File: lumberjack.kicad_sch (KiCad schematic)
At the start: 156 parts

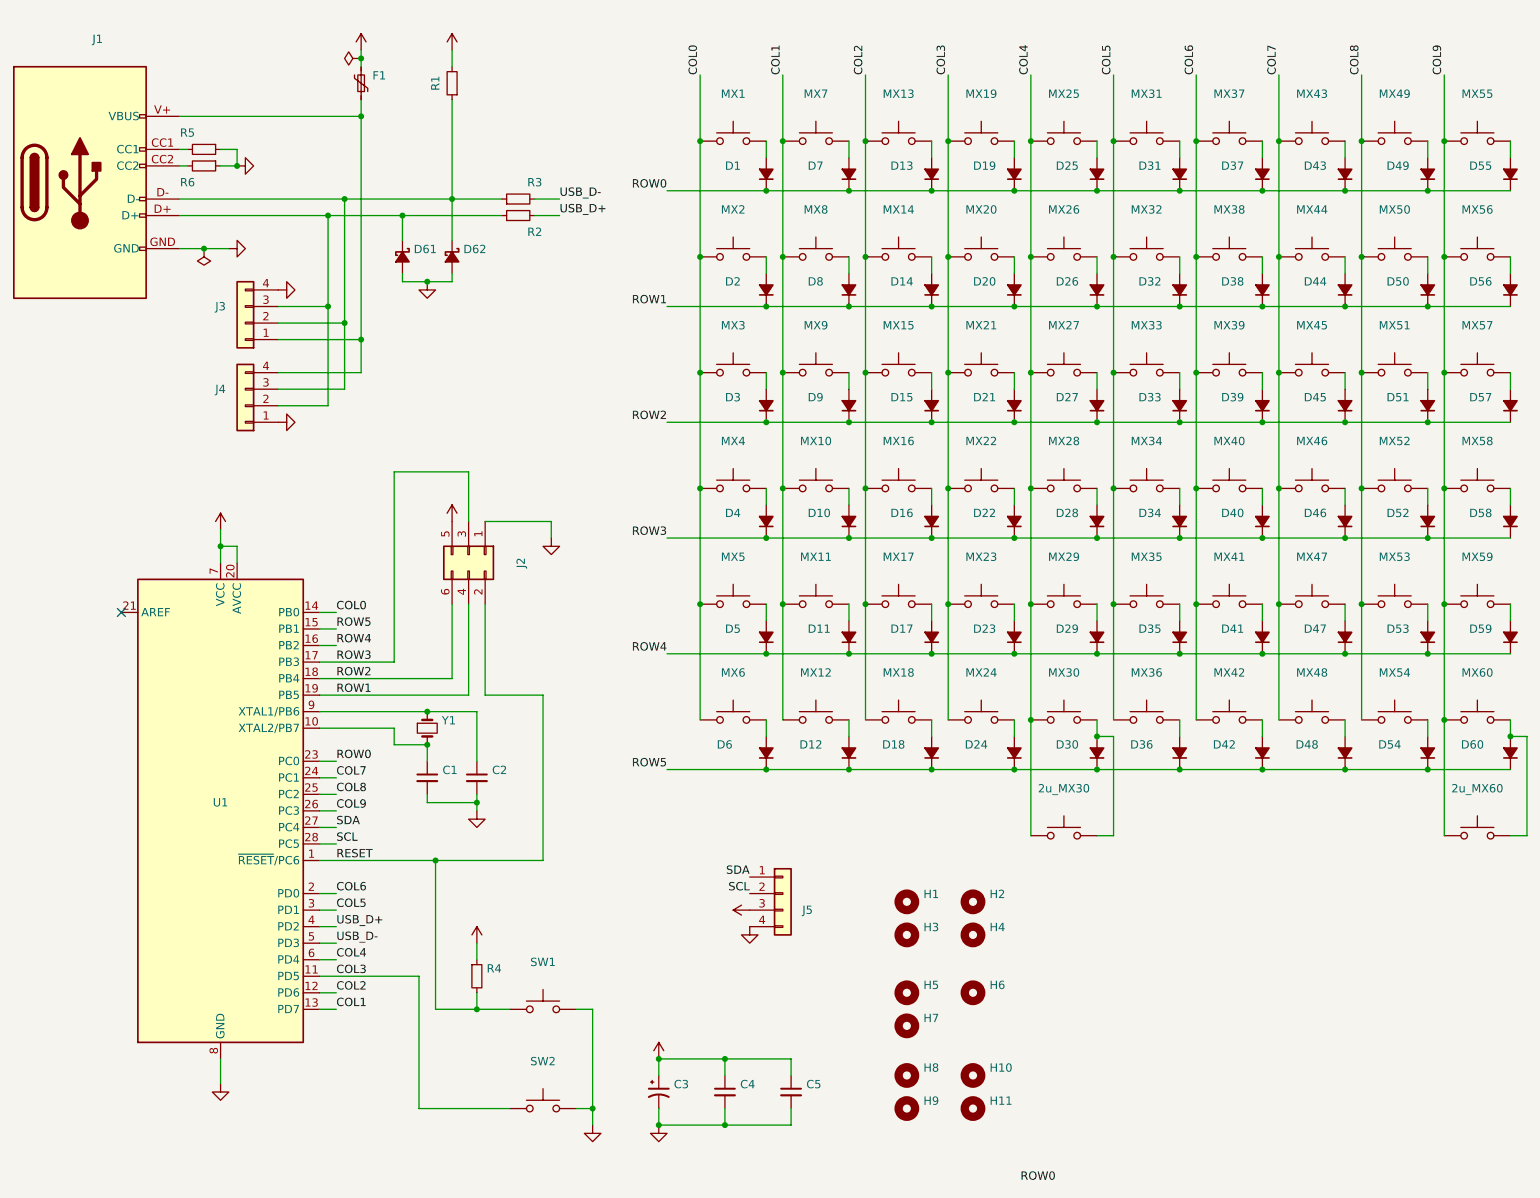
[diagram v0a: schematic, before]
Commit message: Revert to the correct version of the schematic, synchronize PCB with schematic
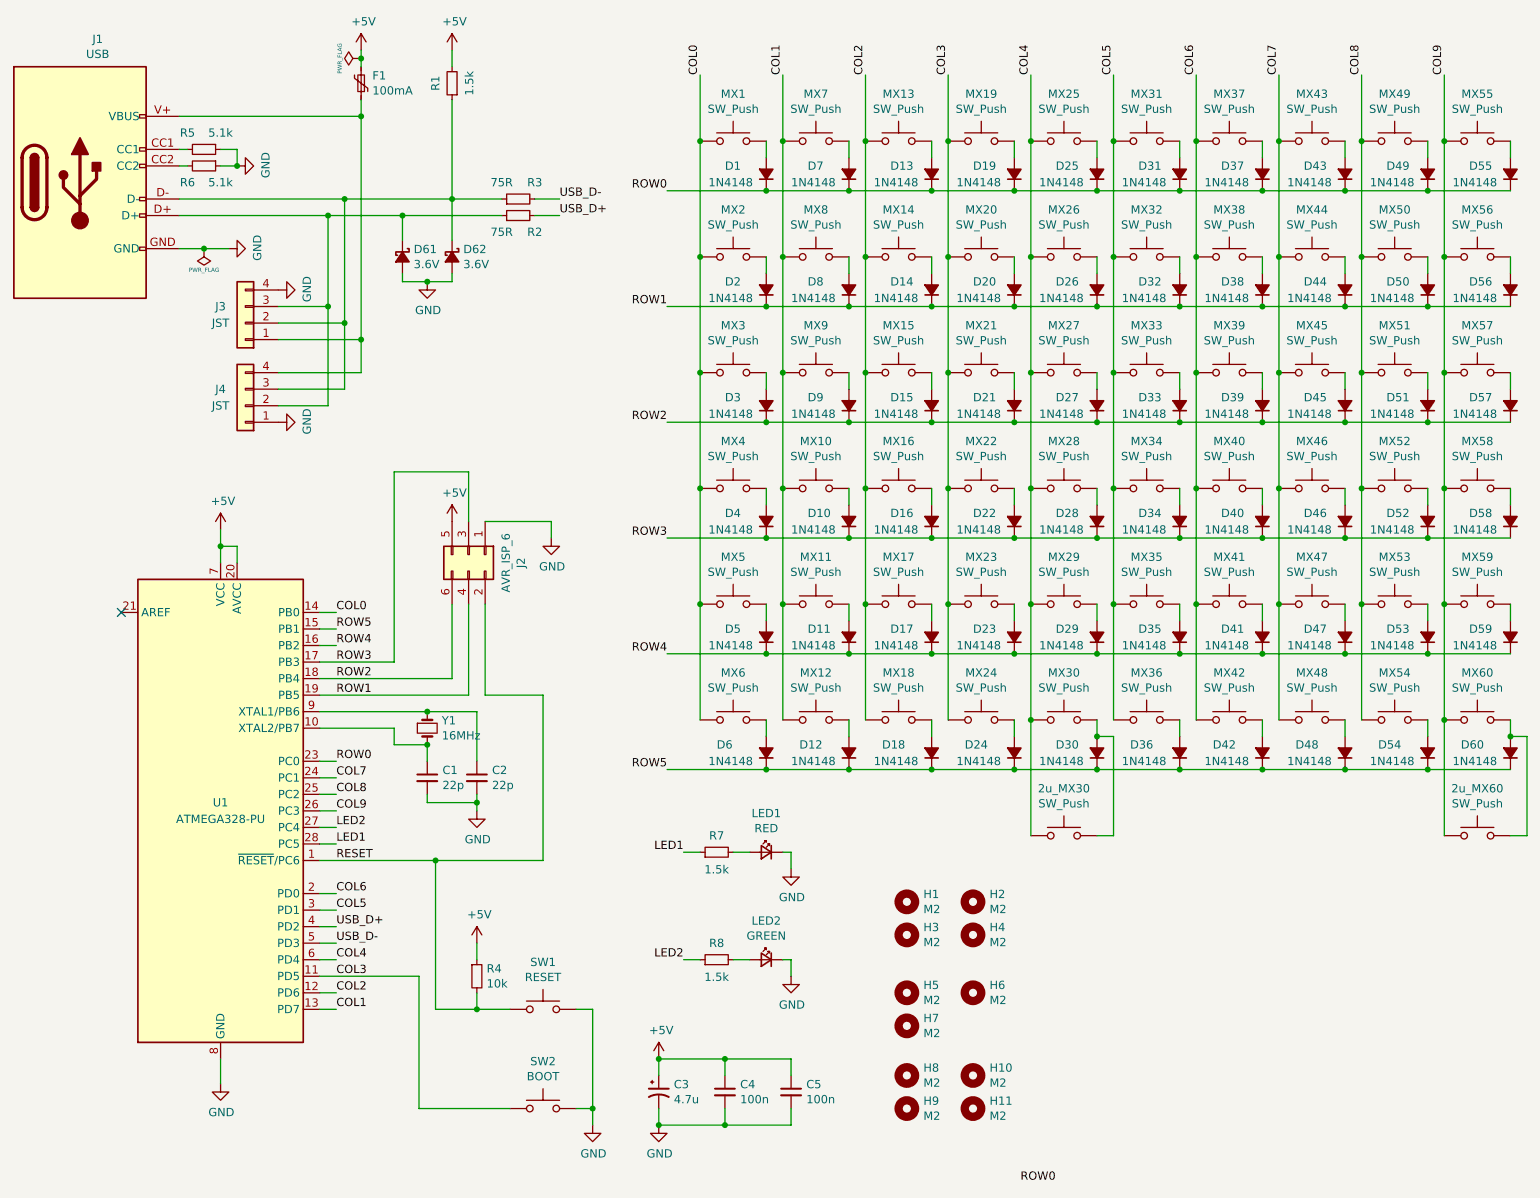
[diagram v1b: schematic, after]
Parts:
- removed J5: (no value), symbol Connector_Generic:Conn_01x04
- added LED1: RED, LED_THT:LED_D3.0mm, symbol Device:LED_Small
- added LED2: GREEN, LED_THT:LED_D3.0mm, symbol Device:LED_Small
- added R7, R8: 1.5k, Resistor_THT:R_Axial_DIN0204_L3.6mm_D1.6mm_P7.62mm_Horizontal, symbol Device:R_Small
- 2u_MX30, 2u_MX60: value (none) -> SW_Push; footprint (none) -> lumberjack:MX_PCB_200B
- C1, C2: value (none) -> 22p; footprint (none) -> Capacitor_THT:C_Disc_D3.0mm_W1.6mm_P2.50mm
- C3: value (none) -> 4.7u; footprint (none) -> Capacitor_THT:CP_Radial_D4.0mm_P1.50mm
- C4, C5: value (none) -> 100n; footprint (none) -> Capacitor_THT:C_Disc_D4.3mm_W1.9mm_P5.00mm
- D1, D10, D11, D12, D13, D14, D15, D16, D17, D18, D19, D2, D20, D21, D22, D23, D24, D25, D26, D27, D28, D29, D3, D30, D31, D32, D33, D34, D35, D36, D37, D38, D39, D4, D40, D41, D42, D43, D44, D45, D46, D47, D48, D49, D5, D50, D51, D52, D53, D54, D55, D56, D57, D58, D59, D6, D60, D7, D8, D9: value (none) -> 1N4148; footprint (none) -> Diode_THT:D_DO-35_SOD27_P7.62mm_Horizontal
- D61, D62: value (none) -> 3.6V; footprint (none) -> Diode_THT:D_DO-35_SOD27_P7.62mm_Horizontal
- F1: value (none) -> 100mA; footprint (none) -> Fuse:Fuse_Bourns_MF-RHT100
- H1, H10, H11, H2, H3, H4, H8, H9: value (none) -> M2; footprint (none) -> lumberjack:MountingHole_M2; now left out of the parts list
- H5, H6, H7: value (none) -> M2; footprint (none) -> lumberjack:MountingSlot_M2; now left out of the parts list
- J1: value (none) -> USB; footprint lumberjack:USB_C_Receptacle_8PIN -> lumberjack:USB_Hybrid
- J2: value (none) -> AVR_ISP_6; footprint (none) -> Connector_PinHeader_2.54mm:PinHeader_2x03_P2.54mm_Vertical
- J3: value (none) -> JST; footprint (none) -> Connector_JST:JST_SH_SM04B-SRSS-TB_1x04-1MP_P1.00mm_Horizontal
- J4: value (none) -> JST; footprint (none) -> lumberjack:S4B-ZRLFSN
- MX1, MX10, MX11, MX12, MX13, MX14, MX15, MX16, MX17, MX18, MX19, MX2, MX20, MX21, MX22, MX23, MX24, MX25, MX26, MX27, MX28, MX29, MX3, MX30, MX31, MX32, MX33, MX34, MX35, MX36, MX37, MX38, MX39, MX4, MX40, MX41, MX42, MX43, MX44, MX45, MX46, MX47, MX48, MX49, MX5, MX50, MX51, MX52, MX53, MX54, MX55, MX56, MX57, MX58, MX59, MX6, MX60, MX7, MX9: value (none) -> SW_Push; footprint lumberjack:MX -> lumberjack:MX_Alps_Choc
- MX8: value (none) -> SW_Push; footprint lumberjack:MX_NTHSTH -> lumberjack:MX_Alps_Choc_NTHSTH
- R1: value (none) -> 1.5k; footprint (none) -> Resistor_THT:R_Axial_DIN0204_L3.6mm_D1.6mm_P7.62mm_Horizontal
- R2, R3: value (none) -> 75R; footprint (none) -> Resistor_THT:R_Axial_DIN0204_L3.6mm_D1.6mm_P7.62mm_Horizontal
- R4: value (none) -> 10k; footprint (none) -> Resistor_THT:R_Axial_DIN0204_L3.6mm_D1.6mm_P7.62mm_Horizontal
- R5, R6: value (none) -> 5.1k; footprint (none) -> Resistor_THT:R_Axial_DIN0204_L3.6mm_D1.6mm_P7.62mm_Horizontal
- SW1: value (none) -> RESET; footprint (none) -> Button_Switch_THT:SW_PUSH_6mm
- SW2: value (none) -> BOOT; footprint (none) -> Button_Switch_THT:SW_PUSH_6mm
- U1: value (none) -> ATMEGA328-PU; footprint (none) -> Package_DIP:DIP-28_W7.62mm
- Y1: value (none) -> 16MHz; footprint (none) -> Crystal:Crystal_HC49-4H_Vertical
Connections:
- net GND: now also LED1.1 (K), LED2.1 (K)
- net SCL renamed LED1
- net LED1: now also R7.1
- net SDA renamed LED2
- net LED2: now also R8.1
- new net: LED2.2 (A), R8.2
- new net: LED1.2 (A), R7.2

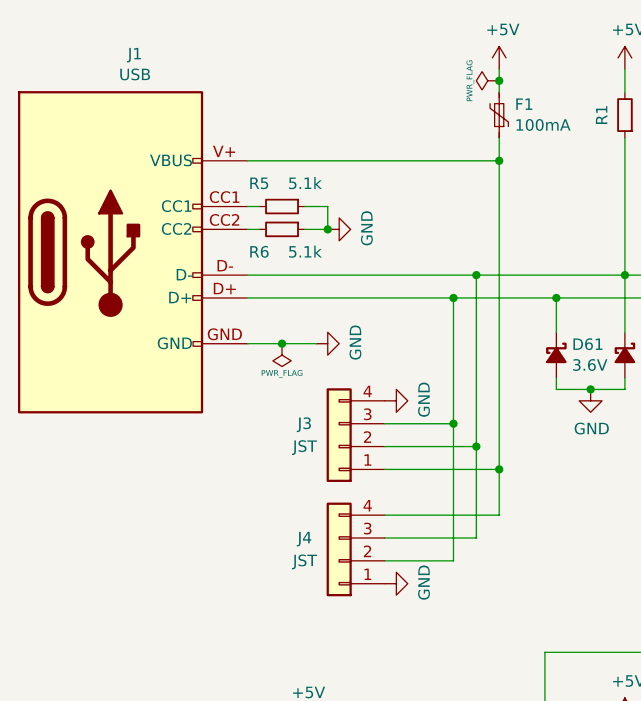
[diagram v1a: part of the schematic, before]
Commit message: Replace hybrid USB footprint with plain USB-C
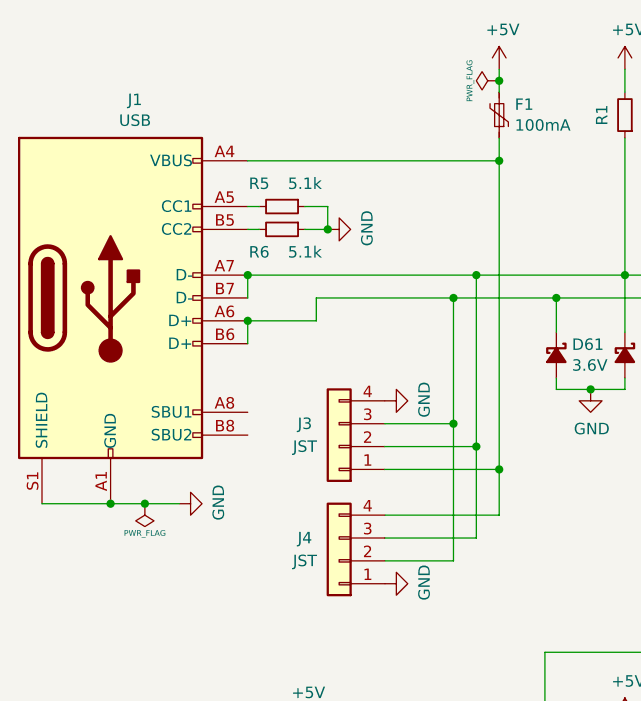
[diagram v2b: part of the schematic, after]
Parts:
- J1: footprint lumberjack:USB_Hybrid -> Connector_USB:USB_C_Receptacle_GCT_USB4085; symbol usb_hybrid:USB_Hybrid -> Connector:USB_C_Receptacle_USB2.0
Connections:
- net GND: now also J1.A1 (GND), J1.A12 (GND), J1.B1 (GND), J1.B12 (GND), J1.S1 (SHIELD); no longer J1.GND
- net at D61.1 (K), J3.3 (Pin_3), J4.2 (Pin_2)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: now also J1.A6 (D+), J1.B6 (D+); no longer J1.D+
- net at D62.1 (K), J3.2 (Pin_2), J4.3 (Pin_3)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: now also J1.A7 (D-), J1.B7 (D-); no longer J1.D-
- net at F1.1, J3.1 (Pin_1), J4.4 (Pin_4): now also J1.A4 (VBUS), J1.A9 (VBUS), J1.B4 (VBUS), J1.B9 (VBUS); no longer J1.V+ (VBUS)
- net at R5.2: now also J1.A5 (CC1); no longer J1.CC1
- net at R6.2: now also J1.B5 (CC2); no longer J1.CC2
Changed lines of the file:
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@@
   (junction (at 198.12 135.89) (diameter 0) (color 0 0 0 0)
   )
+  (junction (at 44.45 53.34) (diameter 0) (color 0 0 0 0)
+  )
   (junction (at 86.36 48.26) (diameter 0) (color 0 0 0 0)
   )
@@
   (junction (at 198.12 64.77) (diameter 0) (color 0 0 0 0)
   )
+  (junction (at 29.21 73.66) (diameter 0) (color 0 0 0 0)
+  )
   (junction (at 213.36 74.93) (diameter 0) (color 0 0 0 0)
   )
@@
   (junction (at 236.22 46.99) (diameter 0) (color 0 0 0 0)
   )
+  (junction (at 44.45 48.26) (diameter 0) (color 0 0 0 0)
+  )
   (junction (at 187.96 39.37) (diameter 0) (color 0 0 0 0)
   )
@@
   (junction (at 236.22 64.77) (diameter 0) (color 0 0 0 0)
   )
-  (junction (at 48.26 55.88) (diameter 0) (color 0 0 0 0)
+  (junction (at 33.02 73.66) (diameter 0) (color 0 0 0 0)
   )
   (junction (at 175.26 128.27) (diameter 0) (color 0 0 0 0)
@@
     (stroke (width 0) (type default) (color 0 0 0 0))
   )
-  (wire (pts (xy 44.45 50.8) (xy 67.31 50.8))
+  (wire (pts (xy 52.07 50.8) (xy 67.31 50.8))
     (stroke (width 0) (type default) (color 0 0 0 0))
   )
@@
     (stroke (width 0) (type default) (color 0 0 0 0))
   )
+  (wire (pts (xy 21.59 73.66) (xy 29.21 73.66))
+    (stroke (width 0) (type default) (color 0 0 0 0))
+  )
   (wire (pts (xy 238.76 92.71) (xy 238.76 110.49))
     (stroke (width 0) (type default) (color 0 0 0 0))
@@
     (stroke (width 0) (type default) (color 0 0 0 0))
   )
+  (wire (pts (xy 52.07 53.34) (xy 52.07 50.8))
+    (stroke (width 0) (type default) (color 0 0 0 0))
+  )
   (wire (pts (xy 185.42 46.99) (xy 198.12 46.99))
     (stroke (width 0) (type default) (color 0 0 0 0))
@@
     (stroke (width 0) (type default) (color 0 0 0 0))
   )
+  (wire (pts (xy 44.45 48.26) (xy 44.45 50.8))
+    (stroke (width 0) (type default) (color 0 0 0 0))
+  )
   (wire (pts (xy 119.38 64.77) (xy 134.62 64.77))
     (stroke (width 0) (type default) (color 0 0 0 0))
@@
     (stroke (width 0) (type default) (color 0 0 0 0))
   )
+  (wire (pts (xy 44.45 53.34) (xy 52.07 53.34))
+    (stroke (width 0) (type default) (color 0 0 0 0))
+  )
   (wire (pts (xy 134.62 82.55) (xy 147.32 82.55))
     (stroke (width 0) (type default) (color 0 0 0 0))
@@
     (stroke (width 0) (type default) (color 0 0 0 0))
   )
-  (wire (pts (xy 44.45 55.88) (xy 48.26 55.88))
+  (wire (pts (xy 29.21 73.66) (xy 33.02 73.66))
     (stroke (width 0) (type default) (color 0 0 0 0))
   )
@@
     (stroke (width 0) (type default) (color 0 0 0 0))
   )
-  (wire (pts (xy 48.26 55.88) (xy 52.07 55.88))
+  (wire (pts (xy 33.02 73.66) (xy 36.83 73.66))
     (stroke (width 0) (type default) (color 0 0 0 0))
   )
@@
     (stroke (width 0) (type default) (color 0 0 0 0))
   )
+  (wire (pts (xy 44.45 53.34) (xy 44.45 55.88))
+    (stroke (width 0) (type default) (color 0 0 0 0))
+  )
   (wire (pts (xy 147.32 100.33) (xy 160.02 100.33))
     (stroke (width 0) (type default) (color 0 0 0 0))
@@
     (pin "2")
   )
-  (symbol (lib_id "power:PWR_FLAG") (at 48.26 55.88 180) (unit 1)
+  (symbol (lib_id "power:PWR_FLAG") (at 33.02 73.66 180) (unit 1)
     (in_bom yes) (on_board yes)
-    (property "Reference" "#FLG02" (id 0) (at 48.26 57.15 0)
+    (property "Reference" "#FLG02" (id 0) (at 33.02 74.93 0)
       (effects (font (size 0.635 0.635)) hide)
     )
-    (property "Value" "PWR_FLAG" (id 1) (at 48.26 59.1566 0)
+    (property "Value" "PWR_FLAG" (id 1) (at 33.02 76.9366 0)
       (effects (font (size 0.635 0.635)))
     )
-    (property "Footprint" "" (id 2) (at 48.26 55.88 0))
-    (property "Datasheet" "" (id 3) (at 48.26 55.88 0))
+    (property "Footprint" "" (id 2) (at 33.02 73.66 0))
+    (property "Datasheet" "" (id 3) (at 33.02 73.66 0))
     (pin "1")
   )
@@
     (pin "4")
   )
-  (symbol (lib_id "usb_hybrid:USB_Hybrid") (at 29.21 45.72 0) (unit 1)
+  (symbol (lib_id "Connector:USB_C_Receptacle_USB2.0") (at 29.21 50.8 0) (unit 1)
     (in_bom yes) (on_board yes)
-    (property "Reference" "J1" (id 0) (at 31.9278 23.6982 0))
-    (property "Value" "USB" (id 1) (at 31.9278 26.0096 0))
-    (property "Footprint" "lumberjack:USB_Hybrid" (id 2) (at 33.02 45.72 0)
-      (effects (font (size 1.27 1.27)) hide)
-    )
-    (property "Datasheet" "https://www.usb.org/sites/default/files/documents/usb_type-c.zip" (id 3) (at 33.02 45.72 0)
-      (effects (font (size 1.27 1.27)) hide)
-    )
-    (pin "CC1")
-    (pin "CC2")
-    (pin "D+")
-    (pin "D-")
-    (pin "GND")
-    (pin "V+")
+    (property "Reference" "J1" (id 0) (at 31.9278 28.7782 0))
+    (property "Value" "USB" (id 1) (at 31.9278 31.0896 0))
+    (property "Footprint" "Connector_USB:USB_C_Receptacle_GCT_USB4085" (id 2) (at 33.02 50.8 0)
+      (effects (font (size 1.27 1.27)) hide)
+    )
+    (property "Datasheet" "https://www.usb.org/sites/default/files/documents/usb_type-c.zip" (id 3) (at 33.02 50.8 0)
+      (effects (font (size 1.27 1.27)) hide)
+    )
+    (pin "A1")
+    (pin "A12")
+    (pin "A4")
+    (pin "A5")
+    (pin "A6")
+    (pin "A7")
+    (pin "A8")
+    (pin "A9")
+    (pin "B1")
+    (pin "B12")
+    (pin "B4")
+    (pin "B5")
+    (pin "B6")
+    (pin "B7")
+    (pin "B8")
+    (pin "B9")
+    (pin "S1")
   )
   (symbol (lib_id "power:GND") (at 59.69 62.23 90) (unit 1)
@@
     (pin "1")
   )
-  (symbol (lib_id "power:GND") (at 52.07 55.88 90) (unit 1)
+  (symbol (lib_id "power:GND") (at 36.83 73.66 90) (unit 1)
     (in_bom yes) (on_board yes)
-    (property "Reference" "#PWR0104" (id 0) (at 58.42 55.88 0)
+    (property "Reference" "#PWR0104" (id 0) (at 43.18 73.66 0)
       (effects (font (size 1.27 1.27)) hide)
     )
-    (property "Value" "GND" (id 1) (at 56.4642 55.753 0))
-    (property "Footprint" "" (id 2) (at 52.07 55.88 0)
+    (property "Value" "GND" (id 1) (at 41.2242 73.533 0))
+    (property "Footprint" "" (id 2) (at 36.83 73.66 0)
       (effects (font (size 1.27 1.27)) hide)
     )
-    (property "Datasheet" "" (id 3) (at 52.07 55.88 0)
+    (property "Datasheet" "" (id 3) (at 36.83 73.66 0)
       (effects (font (size 1.27 1.27)) hide)
     )
@@
     )
     (path "/00000000-0000-0000-0000-0000601e2e5d"
-      (reference "J1") (unit 1) (value "USB") (footprint "lumberjack:USB_Hybrid")
+      (reference "J1") (unit 1) (value "USB") (footprint "Connector_USB:USB_C_Receptacle_GCT_USB4085")
     )
     (path "/00000000-0000-0000-0000-00005c3f2fd0"
